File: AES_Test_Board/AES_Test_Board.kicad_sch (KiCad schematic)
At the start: 37 parts, among them J1 Conn_02x06_Top_Bottom, J2 Conn_02x06_Top_Bottom, J3 Conn_01x02_Pin, U3 TCR3RM10A

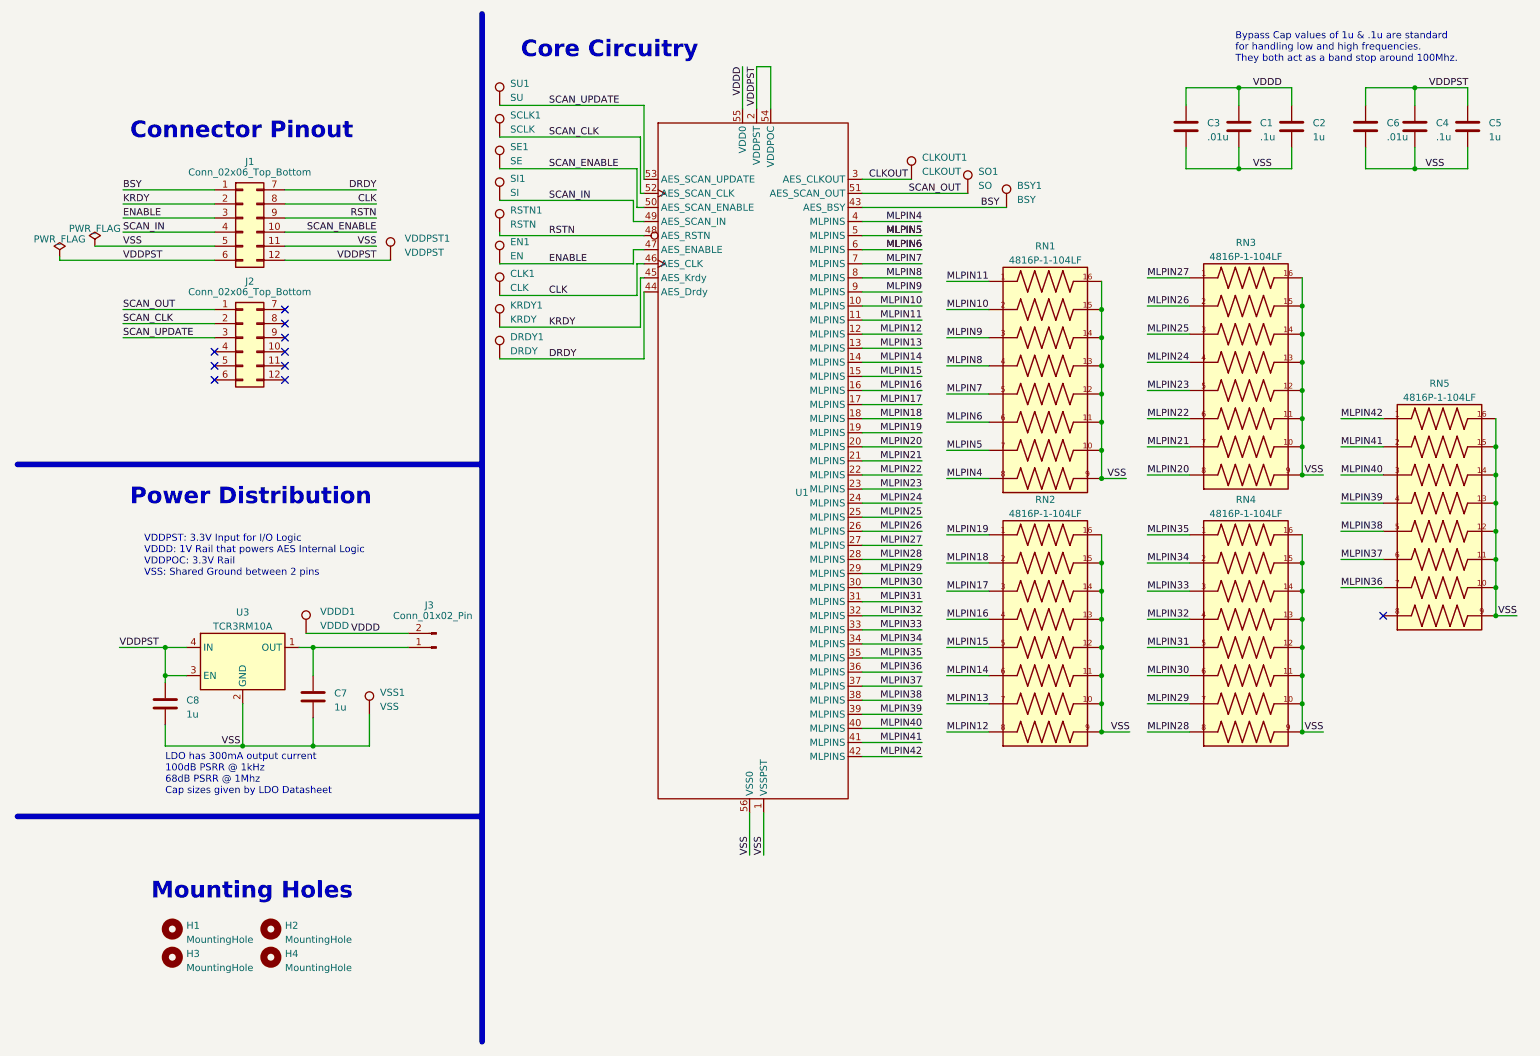
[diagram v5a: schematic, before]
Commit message: Fixed board to match pinout
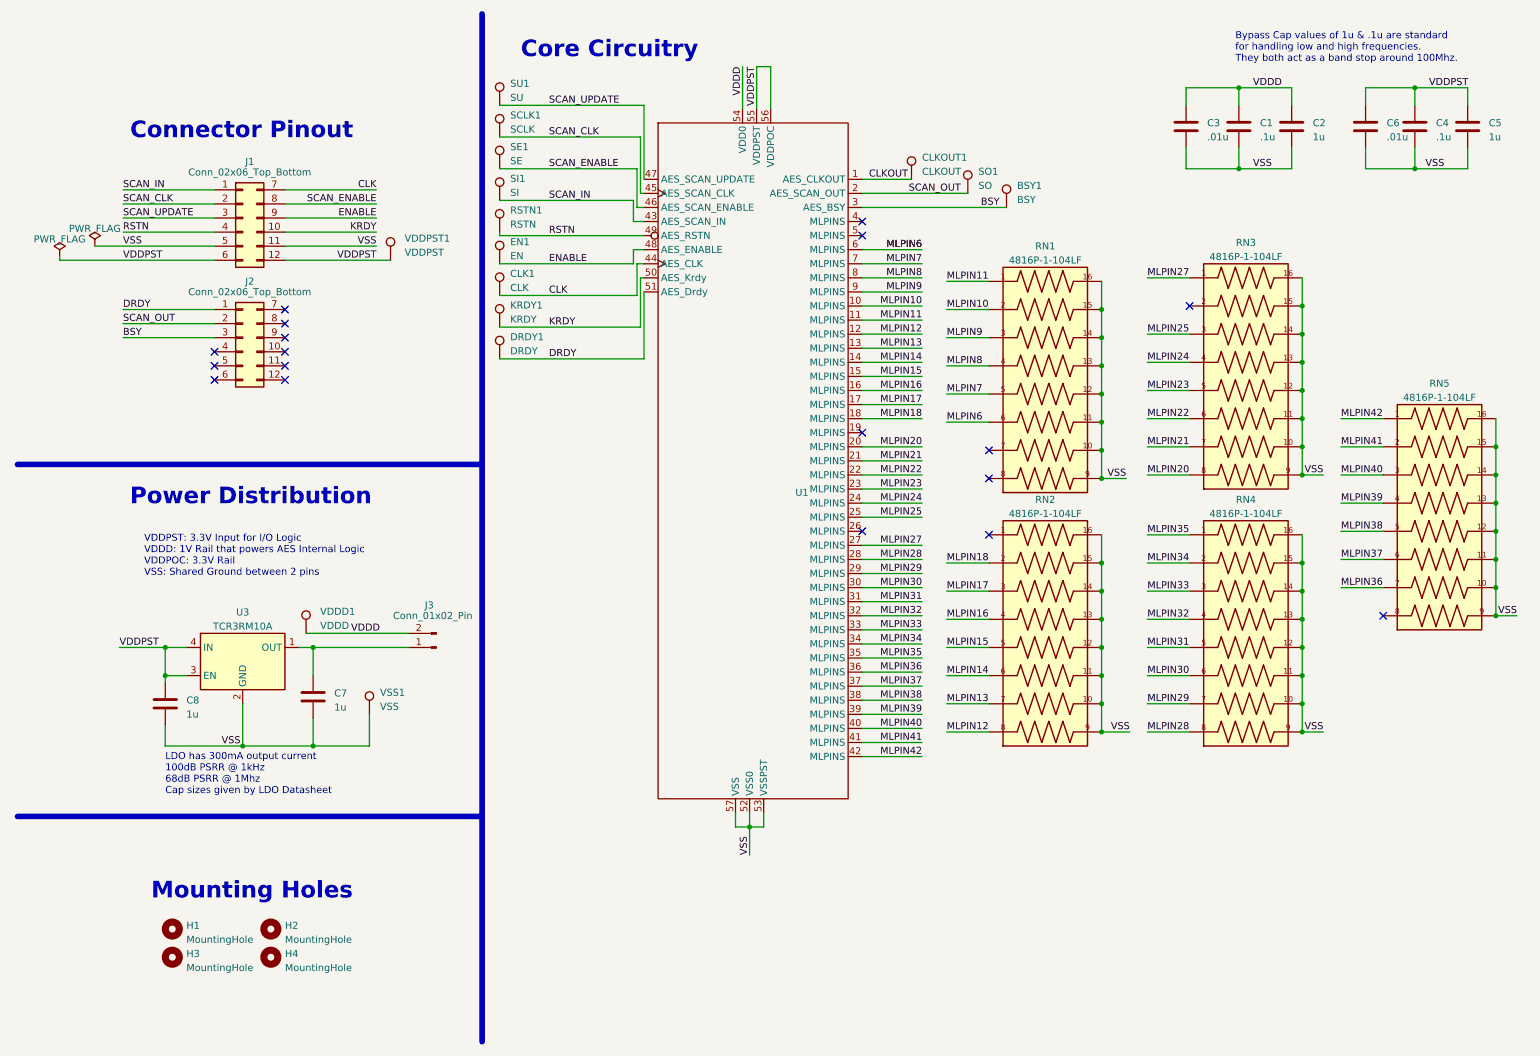
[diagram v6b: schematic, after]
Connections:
- net BSY: now also J2.3 (Pin_3), U1.3 (AES_BSY); no longer J1.1 (Pin_1), U1.43 (AES_BSY)
- net CLK: now also J1.7 (Pin_7), U1.44 (AES_CLK); no longer J1.8 (Pin_8), U1.46 (AES_CLK)
- net CLKOUT: now also U1.1 (AES_CLKOUT); no longer U1.3 (AES_CLKOUT)
- net DRDY: now also J2.1 (Pin_1), U1.51 (AES_Drdy); no longer J1.7 (Pin_7), U1.44 (AES_Drdy)
- net ENABLE: now also J1.9 (Pin_9), U1.48 (AES_ENABLE); no longer J1.3 (Pin_3), U1.47 (AES_ENABLE)
- net KRDY: now also J1.10 (Pin_10), U1.50 (AES_Krdy); no longer J1.2 (Pin_2), U1.45 (AES_Krdy)
- net RSTN: now also J1.4 (Pin_4), U1.49 (AES_RSTN); no longer J1.9 (Pin_9), U1.48 (AES_RSTN)
- net SCAN_CLK: now also J1.2 (Pin_2), U1.45 (AES_SCAN_CLK); no longer J2.2 (Pin_2), U1.52 (AES_SCAN_CLK)
- net SCAN_ENABLE: now also J1.8 (Pin_8), U1.46 (AES_SCAN_ENABLE); no longer J1.10 (Pin_10), U1.50 (AES_SCAN_ENABLE)
- net SCAN_IN: now also J1.1 (Pin_1), U1.43 (AES_SCAN_IN); no longer J1.4 (Pin_4), U1.49 (AES_SCAN_IN)
- net SCAN_OUT: now also J2.2 (Pin_2), U1.2 (AES_SCAN_OUT); no longer J2.1 (Pin_1), U1.51 (AES_SCAN_OUT)
- net SCAN_UPDATE: now also J1.3 (Pin_3), U1.47 (AES_SCAN_UPDATE); no longer J2.3 (Pin_3), U1.53 (AES_SCAN_UPDATE)
- net VDDD: now also U1.54 (VDD0); no longer U1.55 (VDD0)
- net VDDPST: now also U1.55 (VDDPST), U1.56 (VDDPOC); no longer U1.2 (VDDPST), U1.54 (VDDPOC)
- net VSS: now also U1.52 (VSS0), U1.53 (VSSPST), U1.57 (VSS); no longer U1.1 (VSSPST), U1.56 (VSS0)
- net MLPIN19: no longer names the net of RN2.1
- net MLPIN19: no longer U1.19 (MLPINS)
- net MLPIN26: no longer names the net of RN3.2
- net MLPIN26: no longer U1.26 (MLPINS)
- net MLPIN4: no longer names the net of RN1.8
- net MLPIN4: no longer U1.4 (MLPINS)
- net MLPIN5: no longer names the net of RN1.7
- net MLPIN5: no longer U1.5 (MLPINS)
- no-connect marks 10 -> 18

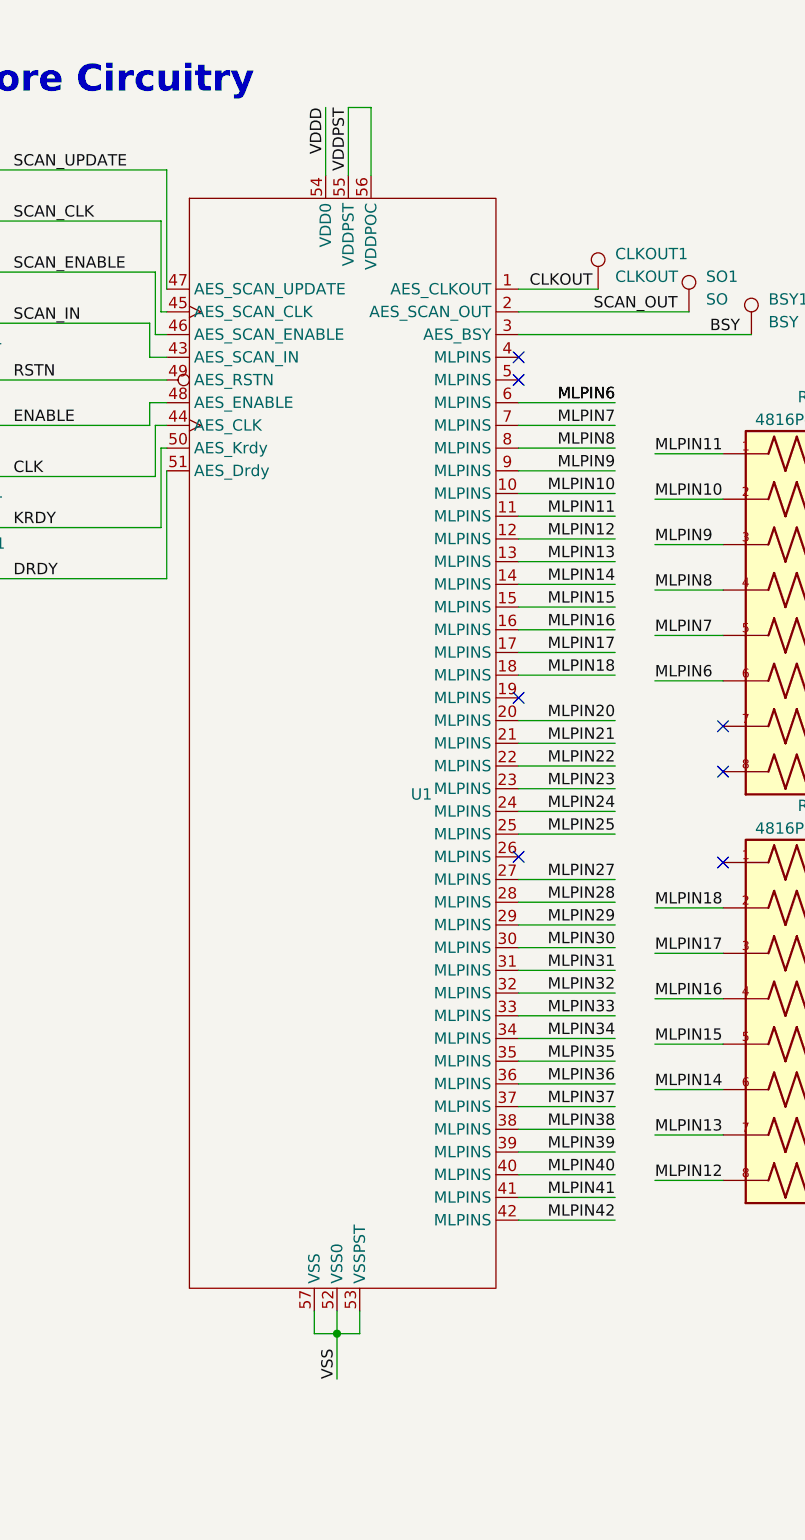
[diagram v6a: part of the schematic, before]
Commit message: Added power pins to connection
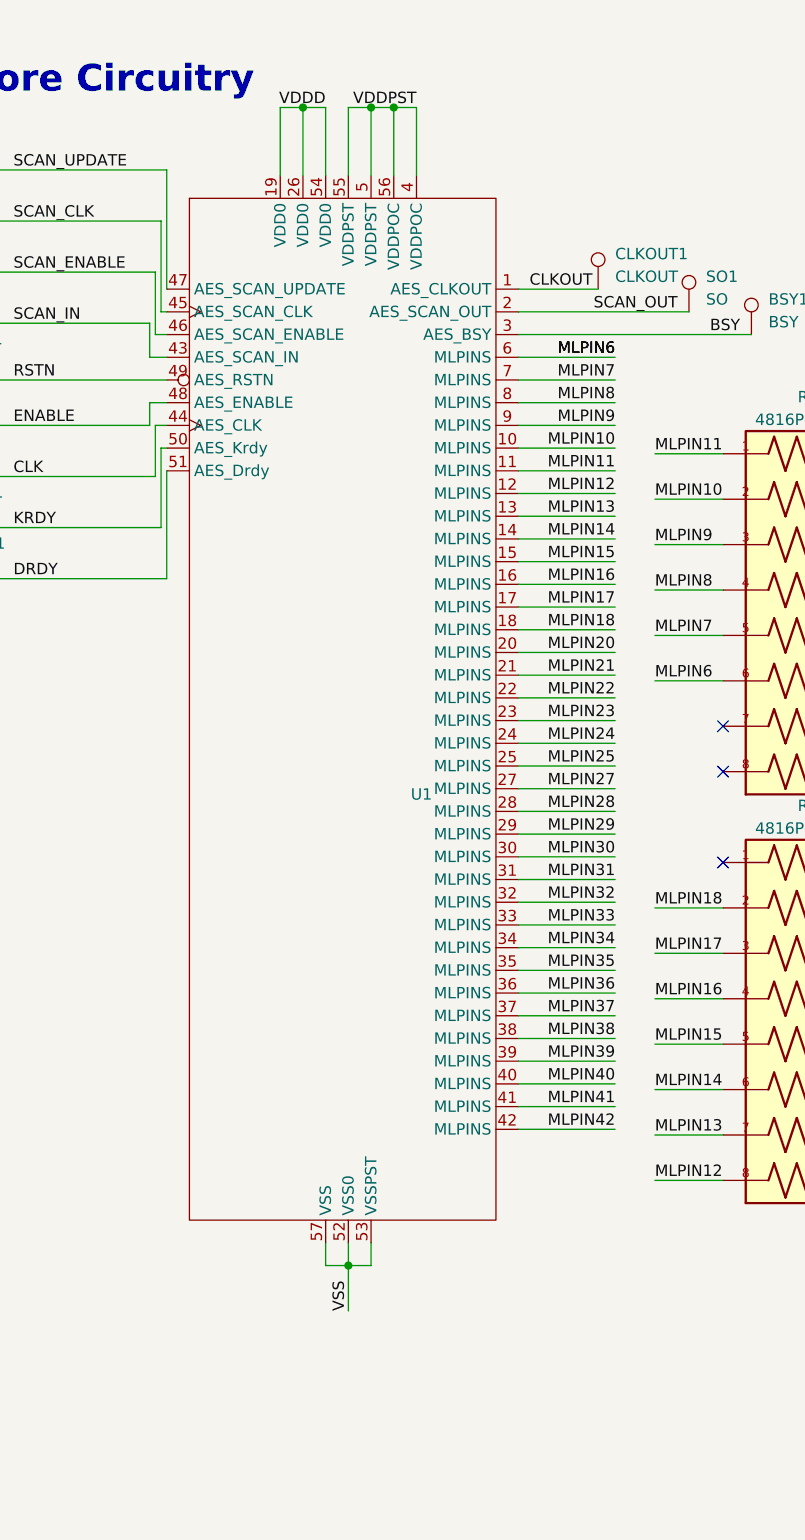
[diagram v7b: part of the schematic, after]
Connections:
- net VDDD: now also U1.19 (VDD0), U1.26 (VDD0)
- net VDDPST: now also U1.4 (VDDPOC), U1.5 (VDDPST)
- no-connect marks 18 -> 14
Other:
- moved on the sheet: U1

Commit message: works nowA
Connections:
- net VSS: now also U1.21 (VSS0), U1.28 (VSS0), U1.6 (VSSPST)
- net MLPIN21: no longer names the net of RN3.7
- net MLPIN21: no longer U1.21 (MLPINS)
- net MLPIN28: no longer names the net of RN4.8
- net MLPIN28: no longer U1.28 (MLPINS)
- net MLPIN6: no longer names the net of RN1.6
- net MLPIN6: no longer U1.6 (MLPINS)
- no-connect marks 14 -> 17
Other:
- moved on the sheet: U1
